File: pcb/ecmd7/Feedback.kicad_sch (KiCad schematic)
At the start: 43 parts, among them U2 MCP33151-05T-E/MN, U4 MCP33151-05T-E/MN, U5 MCP33151-05T-E/MN, U6 TLV71318PDBV, U7 MCP33151-05T-E/MN, U8 MCP33151-05T-E/MN, U9 MCP33151-05T-E/MN

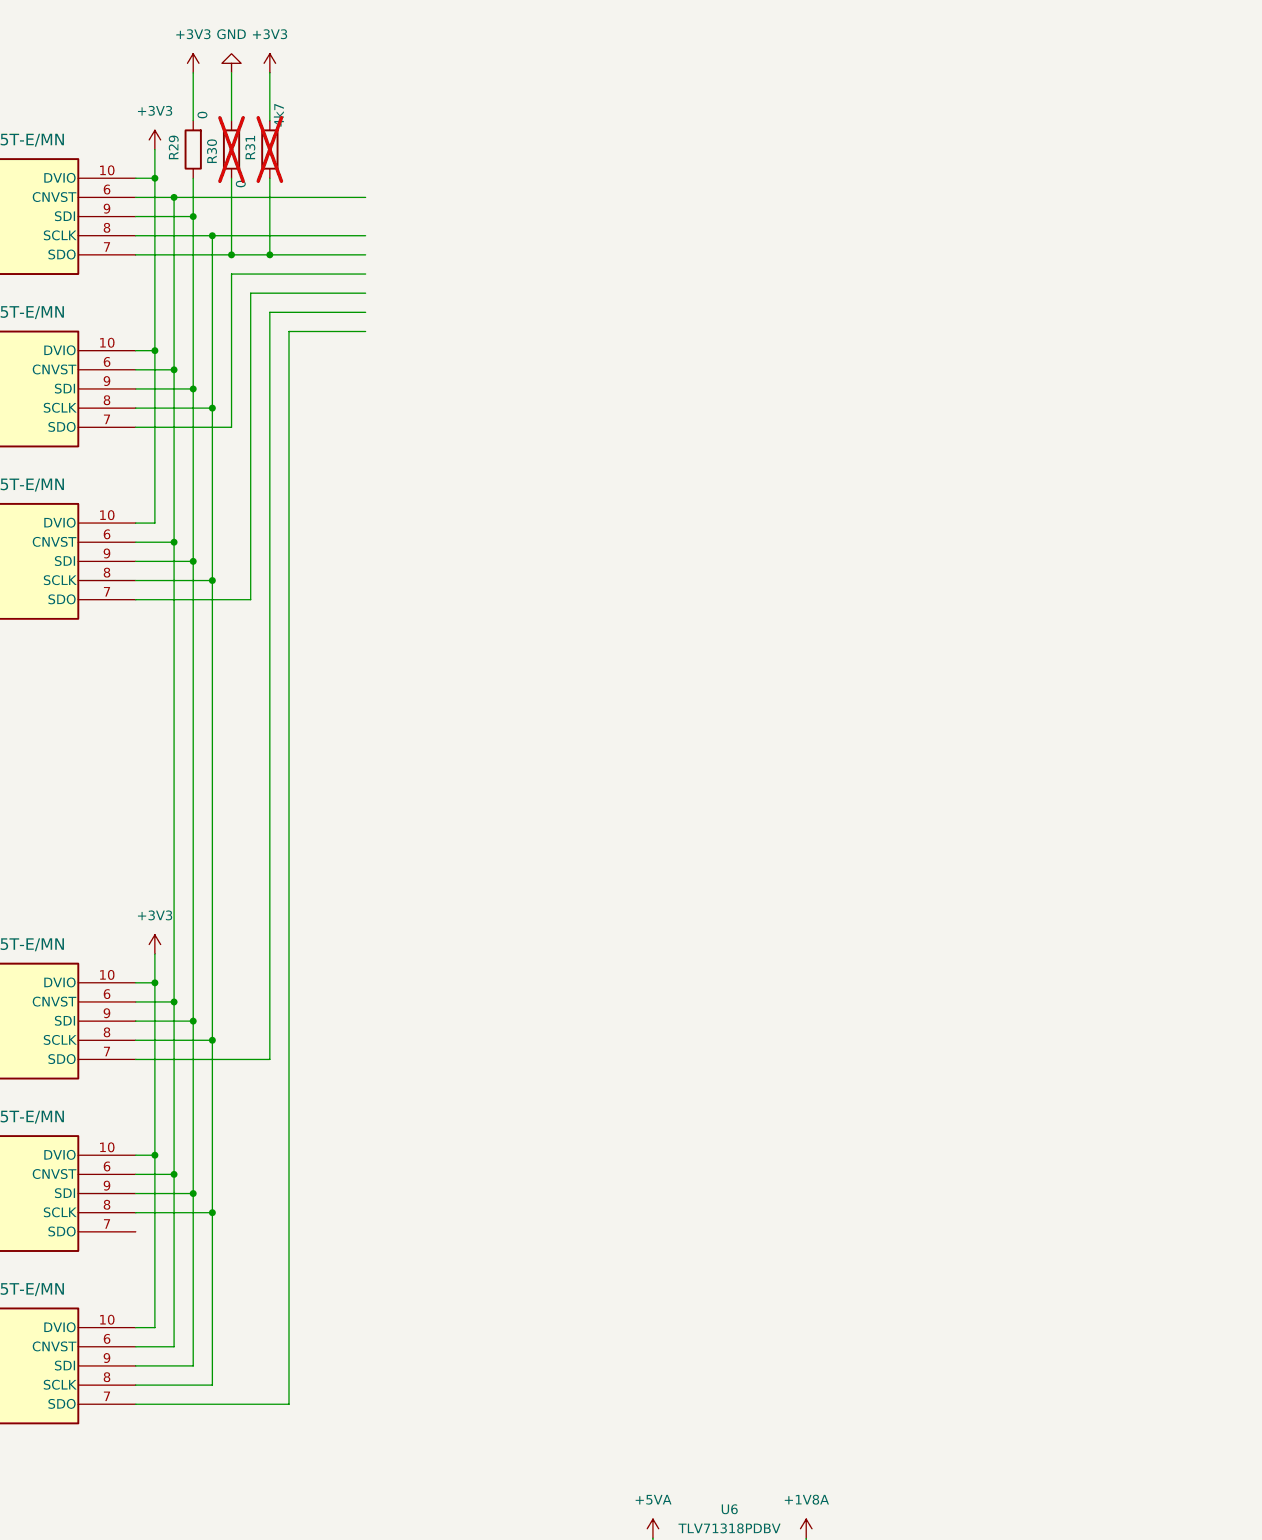
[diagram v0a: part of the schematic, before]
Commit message: WIP: Add sensor interface Re-partition schematic
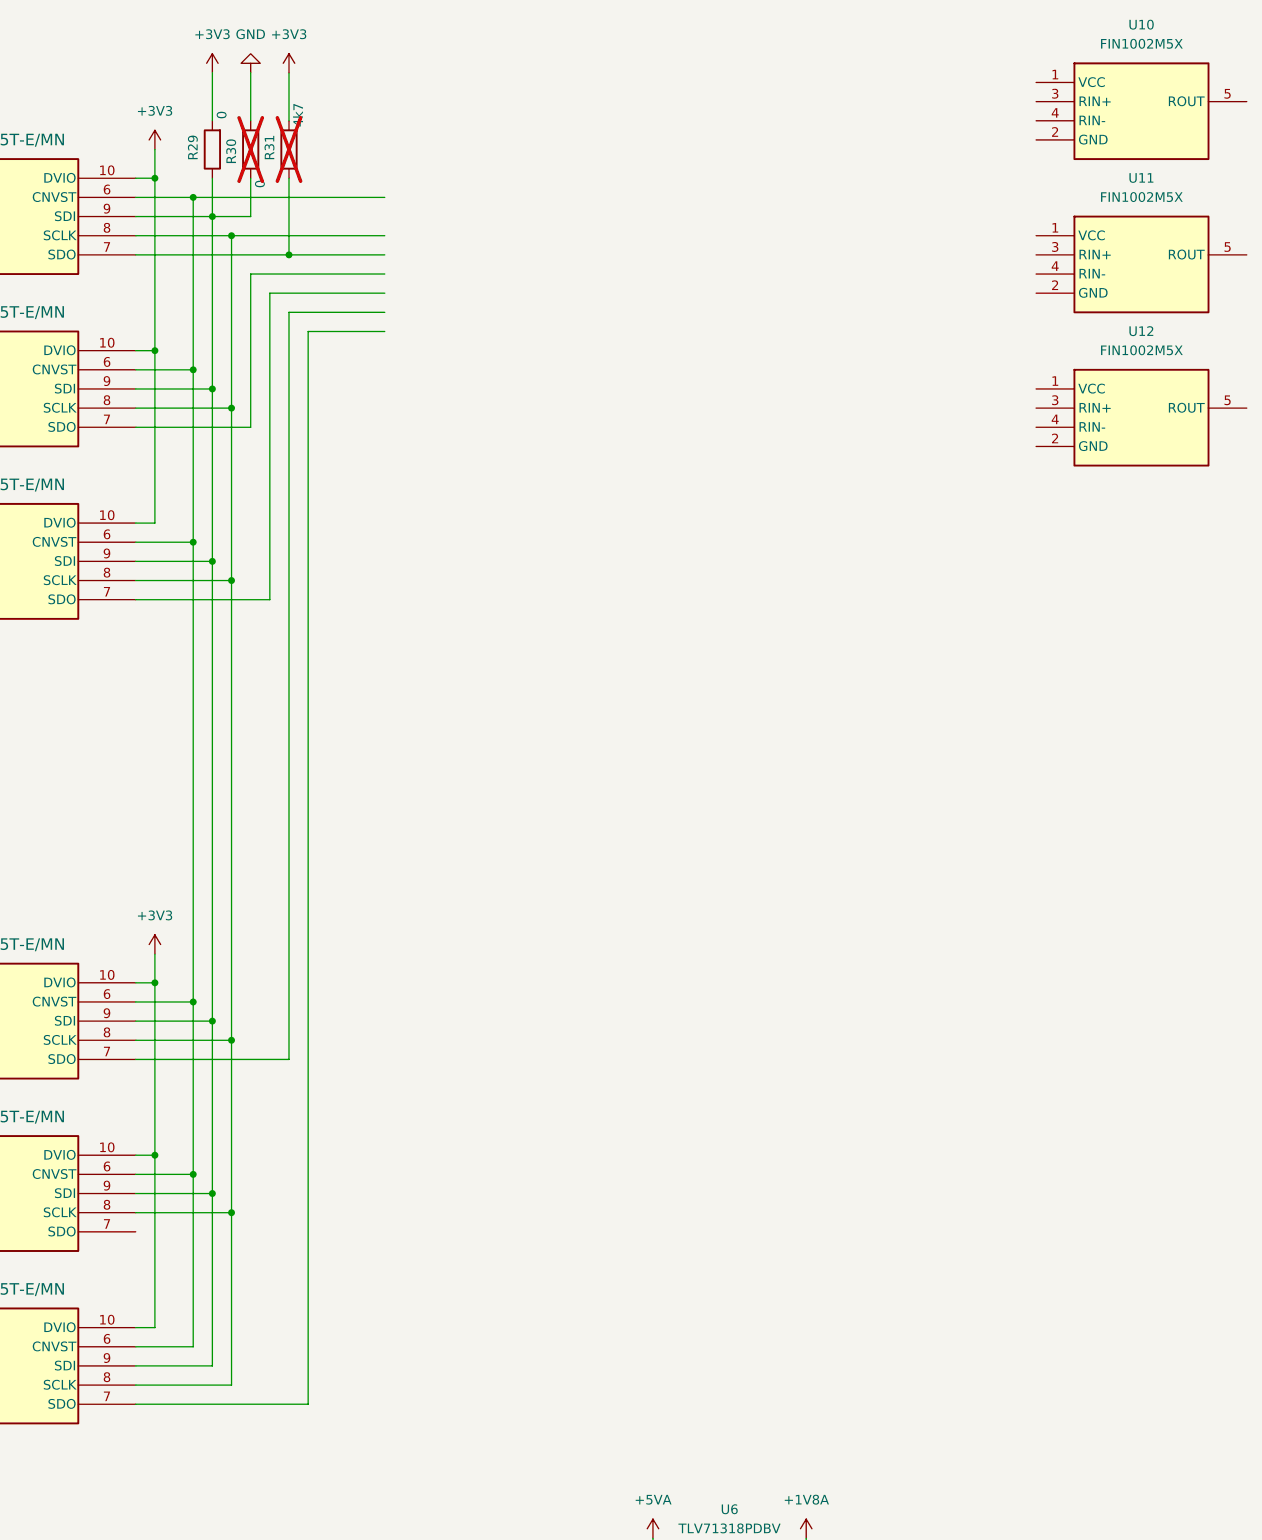
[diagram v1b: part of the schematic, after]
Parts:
- added U10, U11, U12: FIN1002M5X, Package_TO_SOT_SMD:SOT-23-5, symbol ssta_symbols:FIN1002M5X
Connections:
- net at R31.1, U2.7 (SDO): no longer R30.2
- net at R29.1, U2.9 (SDI), U4.9 (SDI)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: now also R30.2
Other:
- title: (none) -> ECMD7 Feedback
- moved on the sheet: R29, R30, R31

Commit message: Finlize schematics
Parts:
- removed C11, C12, C42, C43, C48, C49, C51, C52: 100nF, symbol Device:C
- removed U8, U9: MCP33151-05T-E/MN, TDFN10_MN_MCH, symbol ssta_symbols:MCP33151-05T-E_MN
- added C53: 10nF, symbol Device:C
- added R32, R38, R43: 820, Resistor_SMD:R_0805_2012Metric, symbol Device:R
- added R33, R36, R42: 330, Resistor_SMD:R_0805_2012Metric, symbol Device:R
- added R34, R35, R41: 1.8k, Resistor_SMD:R_0805_2012Metric, symbol Device:R
- added R37: 7.5k, Resistor_SMD:R_0805_2012Metric, symbol Device:R
- added R39, R40: 3.9k, Resistor_SMD:R_0805_2012Metric, symbol Device:R
- added V1: 3.3, symbol Simulation_SPICE:VDC
- added V3: 5, symbol Simulation_SPICE:VDC
- C44, C45, C46: value 22nF -> 2.2nF
- R20: value 100k -> 10k
- R21: value 10k -> 820
- R22, R24: value 100k -> 3.9k
- R23, R25: value 10k -> 3.9k
- R26, R27, R28: value 47 -> 10
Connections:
- net at C41.1, R20.2, R21.1: now also R37.1; no longer U7.3 (AIN+)
- net A_LS_N: now reaches R22.2
- net A_LS_N: now also R24.2, U10.4 (RIN-), U11.4 (RIN-), U12.4 (RIN-), R33.1, R34.2, R35.2, R36.1, R39.2, R41.2, R42.1; no longer R23.1
- net +3.3V: now reaches U10.1 (VCC)
- net +3.3V: now also U11.1 (VCC), U12.1 (VCC), R34.1, R35.1, R41.1, V1.1
- net 0: now reaches U10.2 (GND)
- net 0: now also C1.2, C10.2, C2.2, C3.2, C4.2, C41.2, C44.2, C45.2, C46.2, C47.2, C5.2, C50.2, C6.2, C7.2, C8.2, C9.2, R21.2, R30.1, U11.2 (GND), U12.2 (GND), U2.4 (AIN-), U2.5 (GND), U4.4 (AIN-), U4.5 (GND), U5.4 (AIN-), U5.5 (GND), U6.2 (GND), U7.4 (AIN-), U7.5 (GND), C53.2, R32.2, R38.2, R43.2, V1.2, V3.2
- net A_LS_P: now reaches U10.3 (RIN+)
- net A_LS_P: now also R23.2, R25.2, U11.3 (RIN+), U12.3 (RIN+), R32.1, R33.2, R36.2, R38.1, R40.2, R42.2, R43.1
- net ENC_A: now reaches U10.5 (ROUT)
- net ENC_BP: now reaches R25.1
- net ENC_BP: no longer R24.2
- net ENC_Z: now reaches U12.5 (ROUT)
- net CS_AD: now reaches U2.6 (CNVST), U4.6 (CNVST), U5.6 (CNVST), U7.6 (CNVST)
- net AD_SCK: now reaches U2.8 (SCLK), U4.8 (SCLK), U5.8 (SCLK), U7.8 (SCLK)
- net AD_SDO_IU: now reaches R31.1, U2.7 (SDO)
- net ENC_B: now reaches U11.5 (ROUT)
- net AD_SDO_IV: now reaches U4.7 (SDO)
- net AD_SDO_VBUS: now reaches U7.7 (SDO)
- net AD_SDO_IW: now reaches U5.7 (SDO)
- net CURU renamed I_U
- net CURV renamed I_V
- net CURW renamed I_W
- removed net GND: C1.2, C10.2, C2.2, C3.2, C4.2, C41.2, C44.2, C45.2, C46.2, C47.2, C5.2, C50.2, C6.2, C7.2, C8.2, C9.2, R21.2, R23.2, R25.2, R30.1, U2.4 (AIN-), U2.5 (GND), U4.4 (AIN-), U4.5 (GND), U5.4 (AIN-), U5.5 (GND), U6.2 (GND), U7.4 (AIN-), U7.5 (GND)
- net VU renamed VMot
- net VV renamed ENC_AN
- net VW renamed ENC_BN
- new net: C53.1, R37.2, U7.3 (AIN+)
- new net A_N: V3.1
- new net ENC_AP: R23.1
- new net ENC_ZN: R39.1
- new net ENC_ZP: R40.1
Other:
- moved on the sheet: C1, C10, C2, C3, C4, C44, C45, C46, C47, C5, C50, C6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
